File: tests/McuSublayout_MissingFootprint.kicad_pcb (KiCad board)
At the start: 2 copper layers, 6 parts, among them J2 PinHeader1.27 Shrouded 2x5, U2 STM32F103xxT6

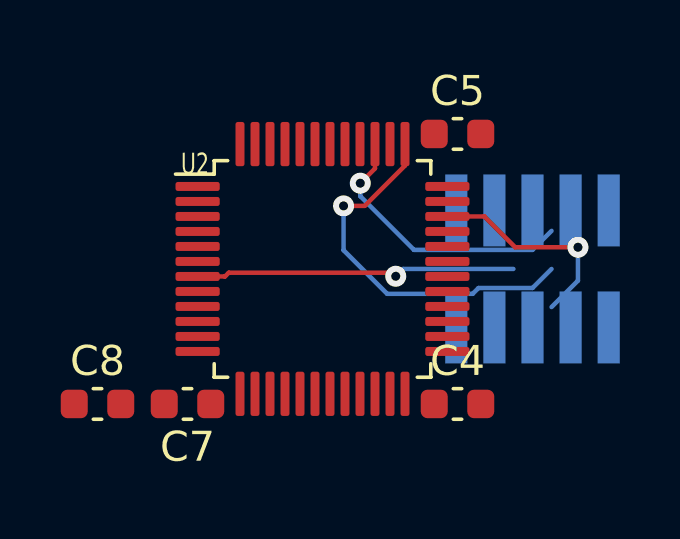
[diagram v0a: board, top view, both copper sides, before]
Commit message: Add more test cases (#5)
Adds a MCU sublayout with crystal but missing SWD. Test checks for
success (non-crashing)

Add a dummy unique net to the extra footprint sublayout test. Deletes
the SWD header (in addition to the caps) from the missing footprint
test.
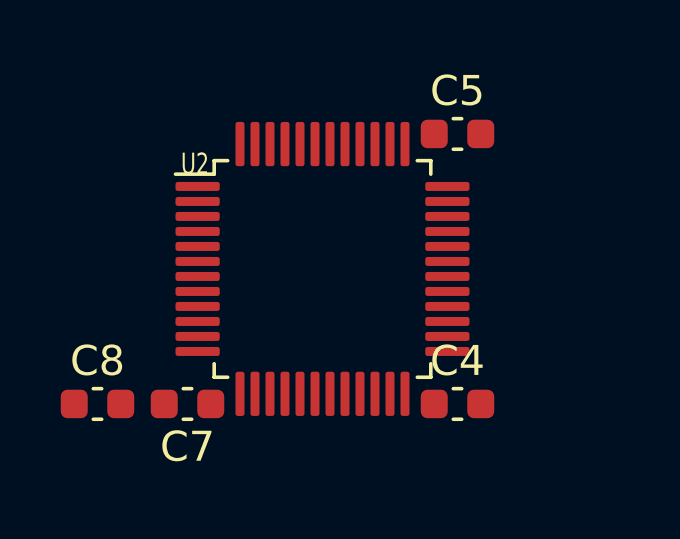
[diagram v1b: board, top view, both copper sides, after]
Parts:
- removed J2: PinHeader1.27 Shrouded 2x5, Connector_PinHeader_1.27mm:PinHeader_2x05_P1.27mm_Vertical_SMD
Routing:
- net mcu.swd_node.swclk: track 12.7 -> 0.00 mm, vias 1 -> 0
- net mcu.reset_node: track 10.7 -> 0.00 mm, vias 1 -> 0
- net mcu.swd.swo: track 9.32 -> 0.00 mm, vias 1 -> 0
- net mcu.swd_node.swdio: track 7.14 -> 0.00 mm, vias 1 -> 0
